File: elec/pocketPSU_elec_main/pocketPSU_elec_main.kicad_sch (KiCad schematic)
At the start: 4 parts

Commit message: mid-layout
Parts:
- H1, H2, H3, H4: now not fitted
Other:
- removed sheet usb_coms

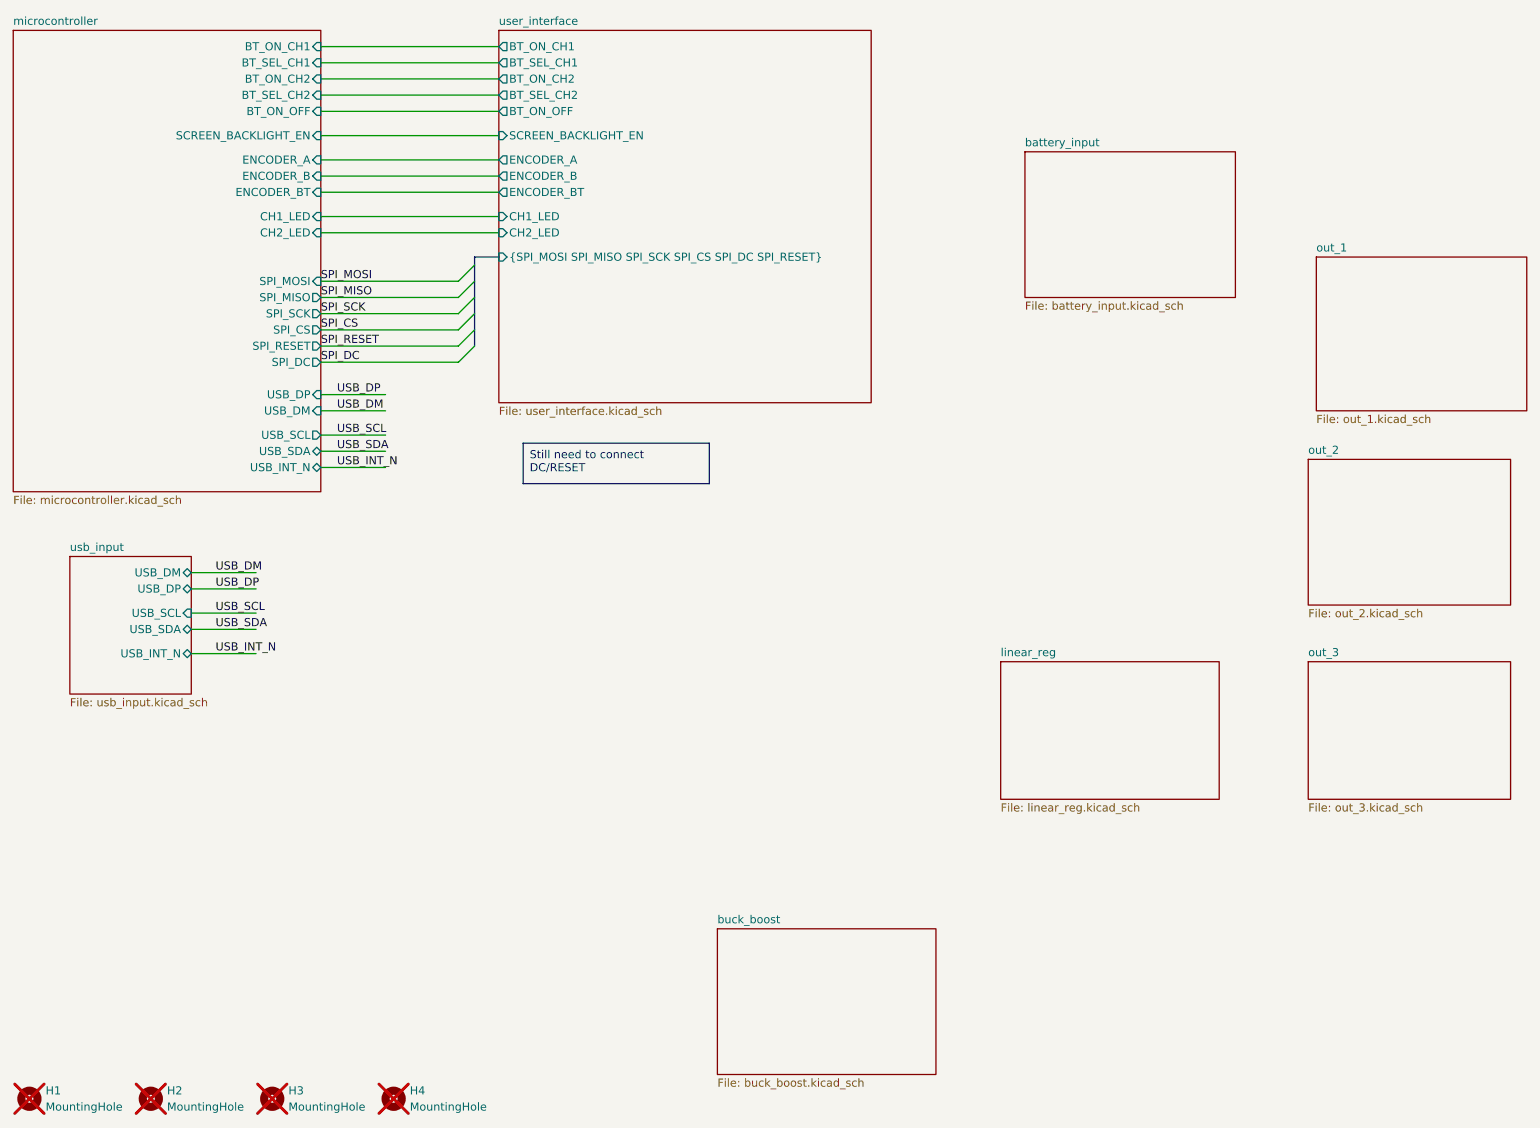
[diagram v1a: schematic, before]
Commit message: make flex pcb for lcd fix
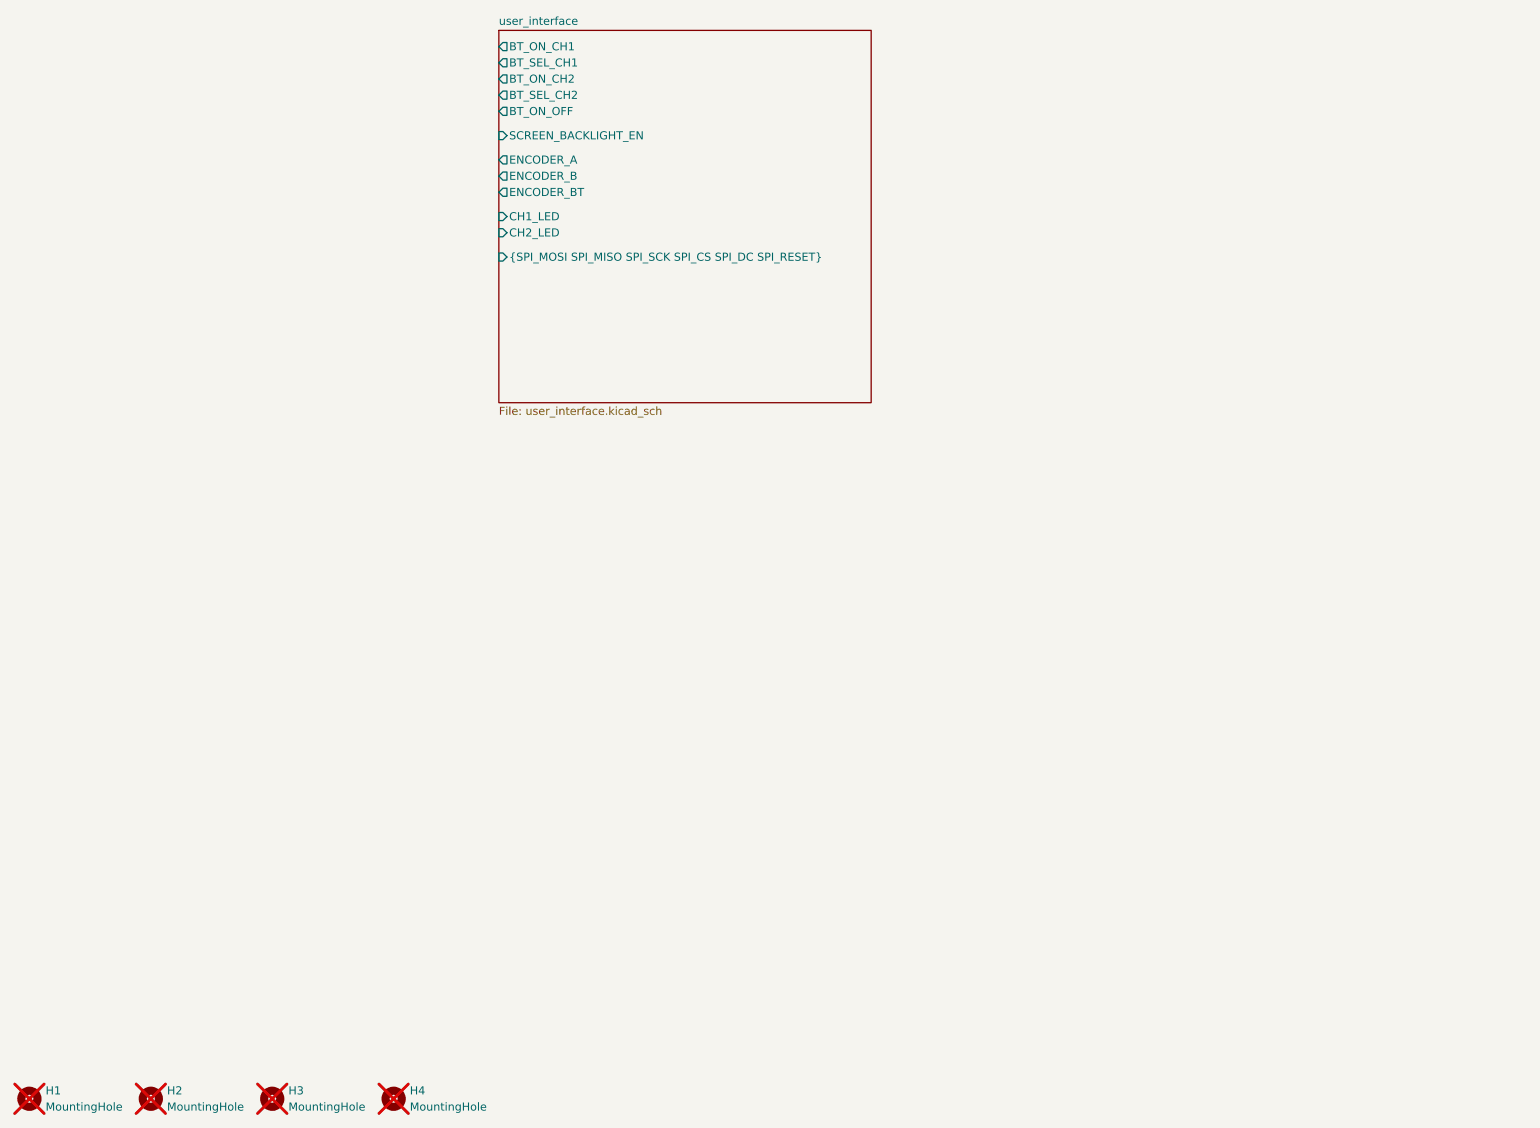
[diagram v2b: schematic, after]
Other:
- removed sheet battery_input
- removed sheet buck_boost
- removed sheet linear_reg
- removed sheet microcontroller
- removed sheet out_1
- removed sheet out_2
- removed sheet out_3
- removed sheet usb_input
